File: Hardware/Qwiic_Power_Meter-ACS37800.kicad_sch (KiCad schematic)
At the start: 31 parts, among them J1 Conn_01x01, J10 Conn_01x01, J11 Conn_01x01, J2 Conn_01x04, J3 Qwiic_RA, J4 HI, J5 LO, J6 Conn_01x01, J7 Qwiic_RA, J8 Conn_01x01, J9 Conn_01x01, U1 ACS37800

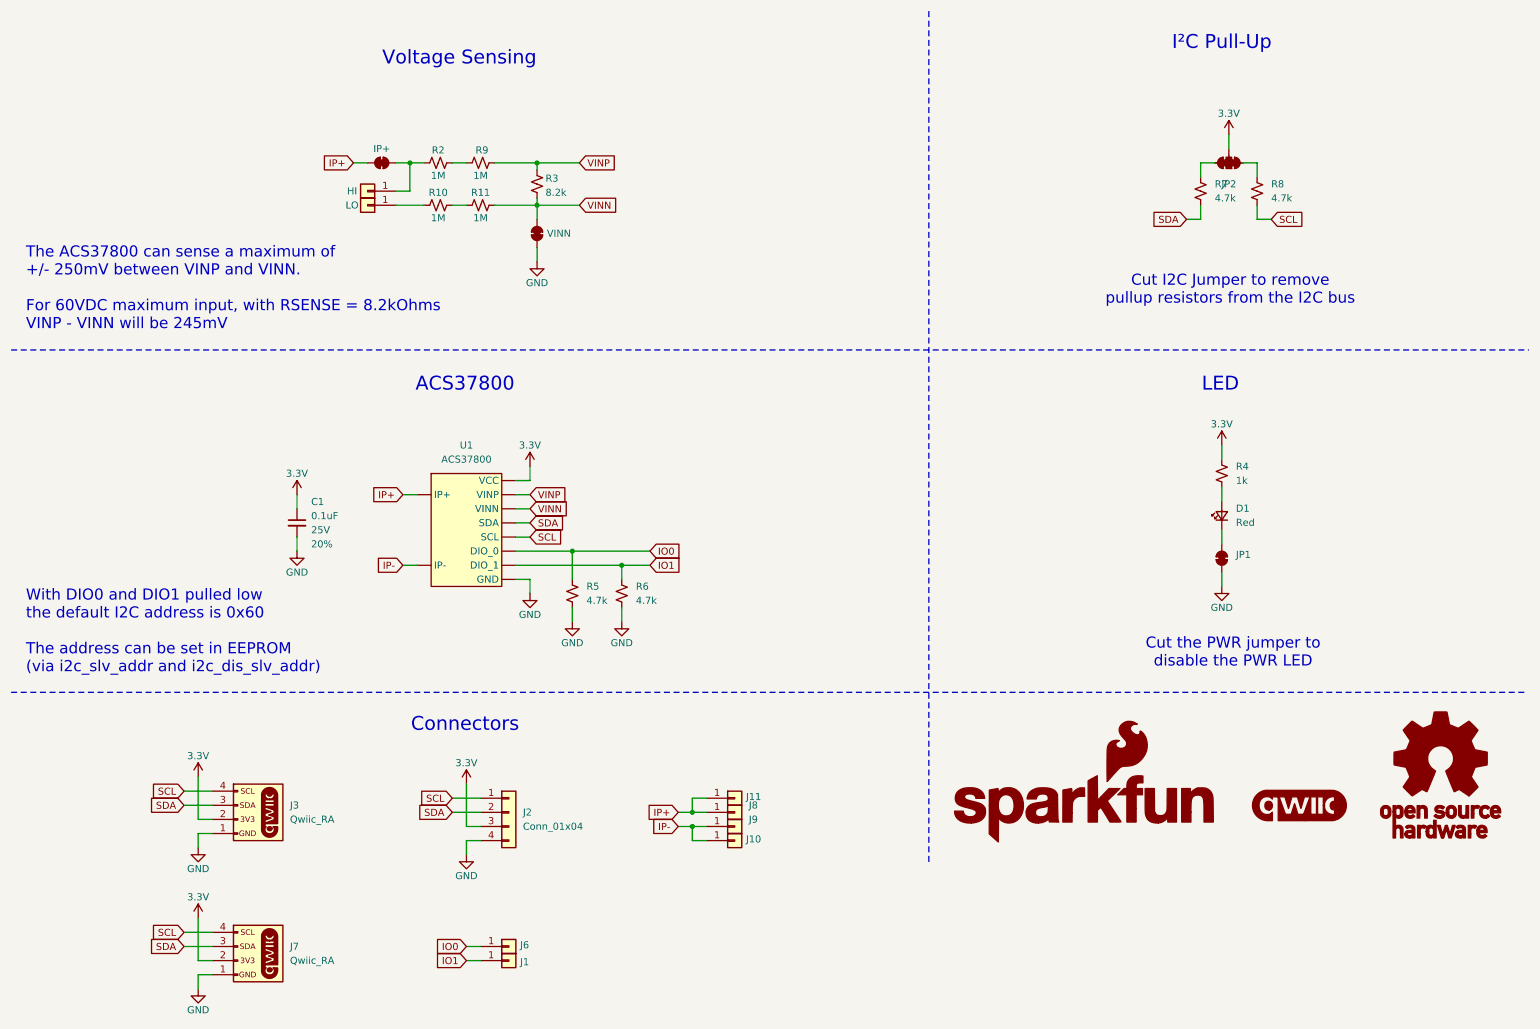
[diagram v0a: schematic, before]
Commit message: Update SOIC Wide footprint
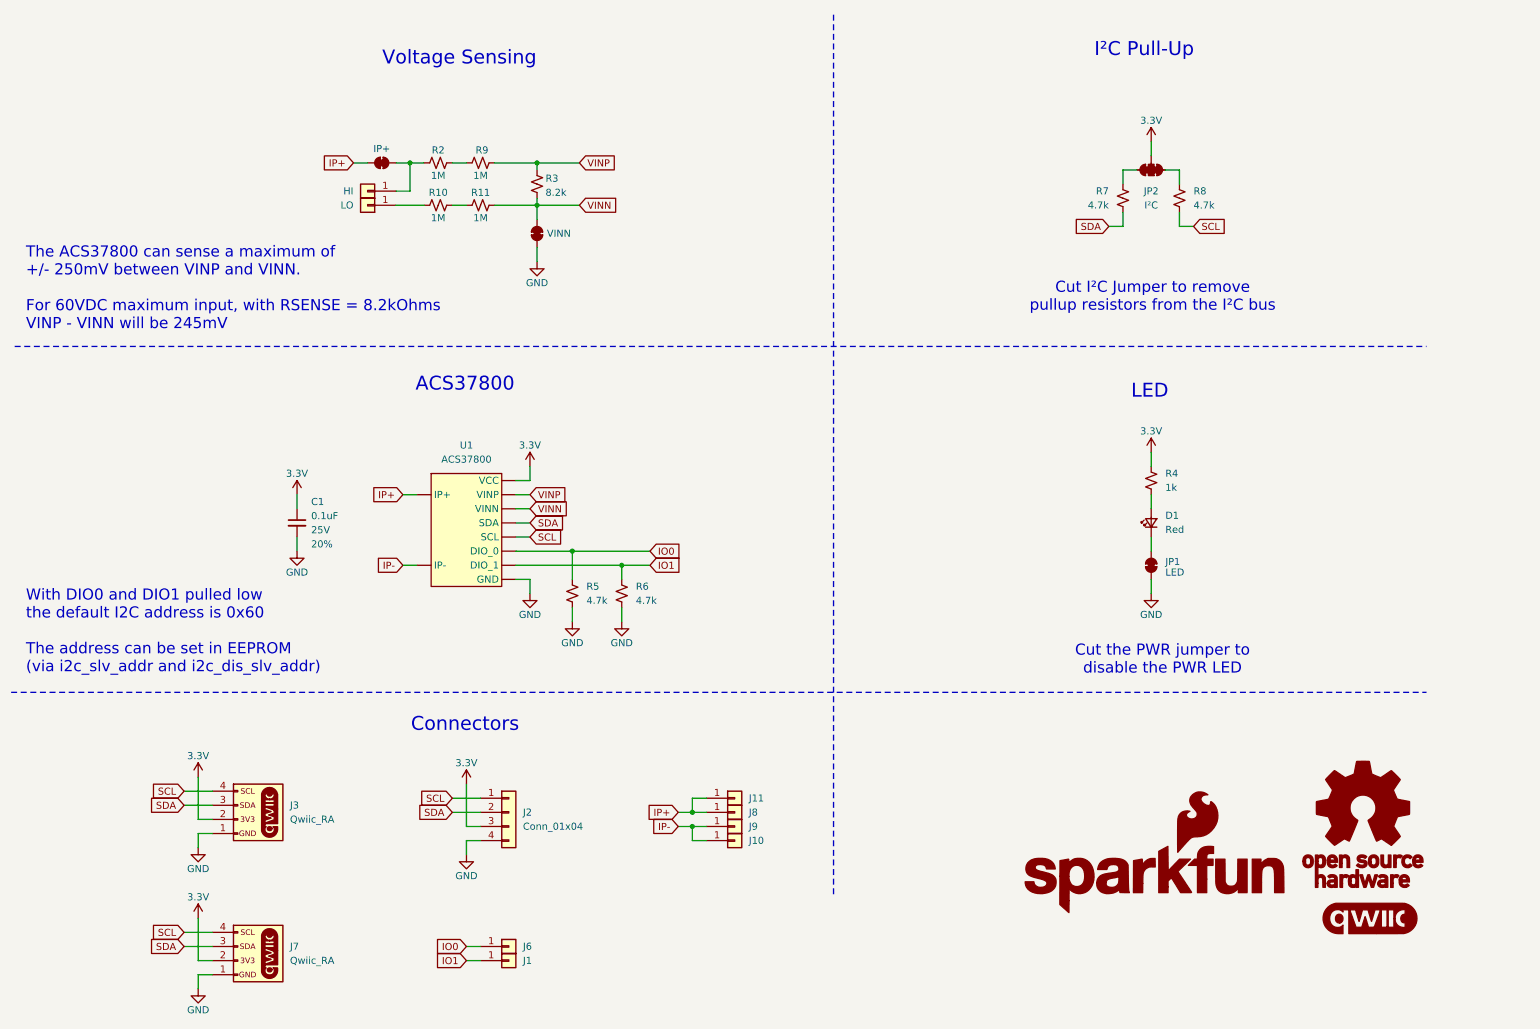
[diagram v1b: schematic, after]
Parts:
- JP1: value ~ -> LED
- JP2: value ~ -> I²C
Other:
- note added: "Cut I²C Jumper to remove pullup resistors from the I²C bus"
- note removed: "Cut I2C Jumper to remove pullup resistors from the I2C bus"
- title: Qwiic Power Meter ACS37800 -> SparkFun Qwiic Power Meter ACS37800
- moved on the sheet: D1, JP1, JP2, R4, R7, R8

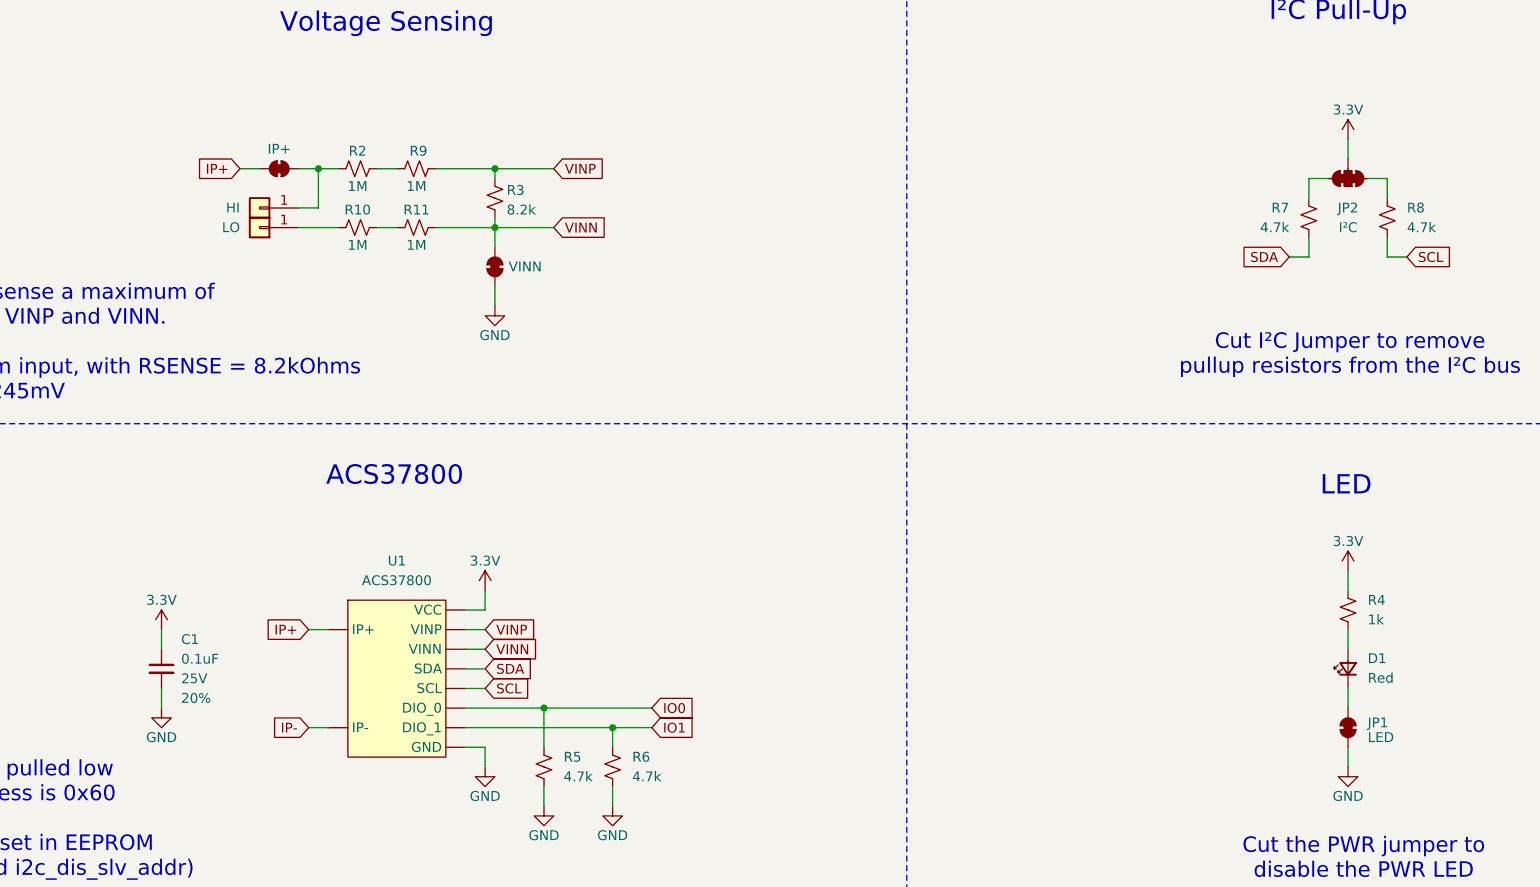
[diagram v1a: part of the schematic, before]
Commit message: Update 0.4in symbol and FP
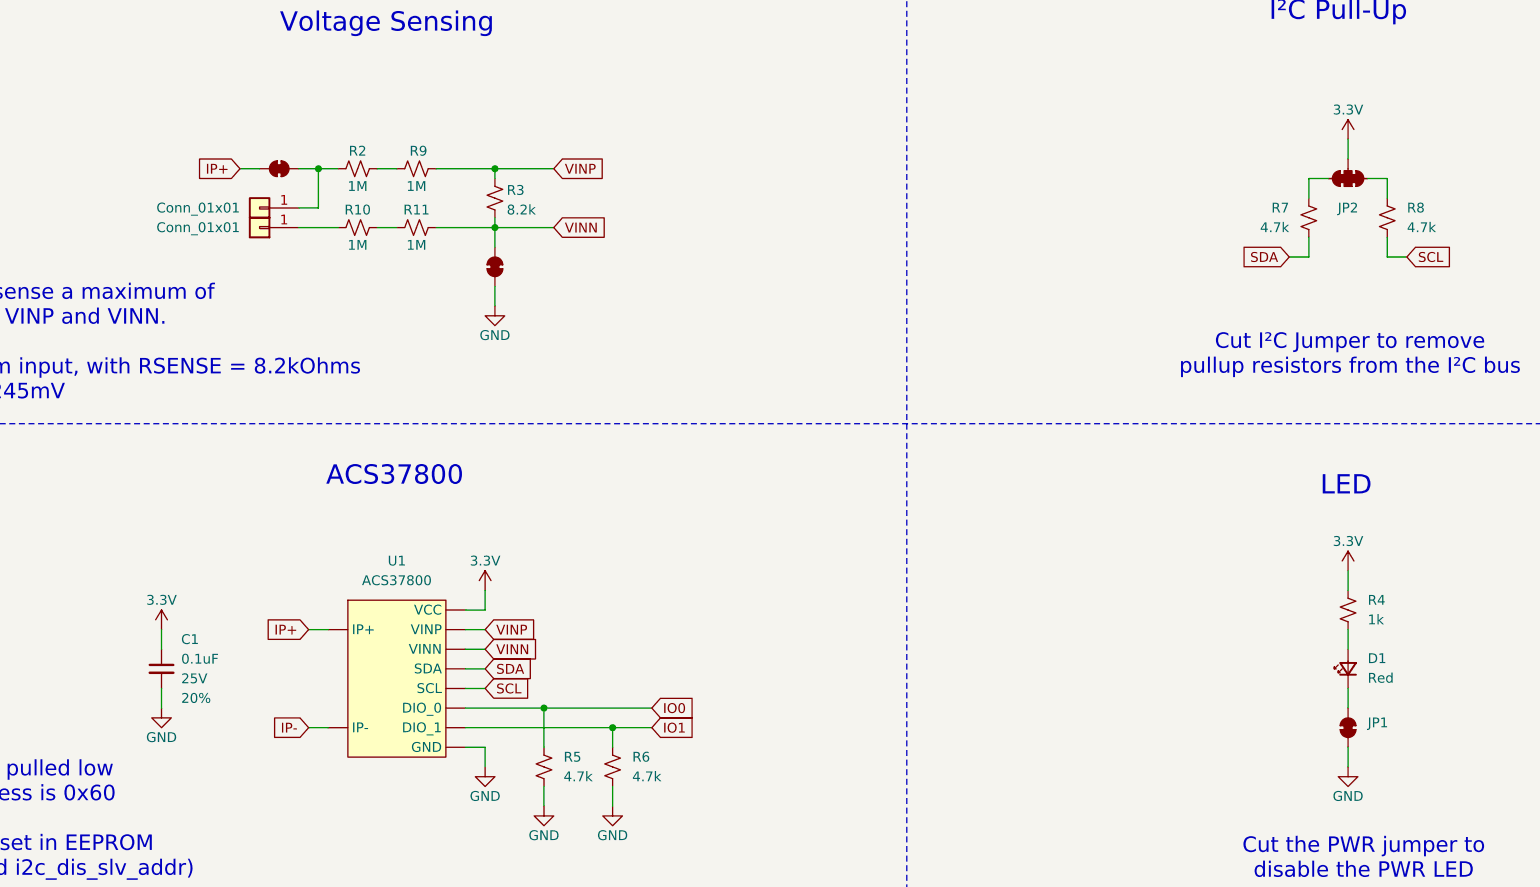
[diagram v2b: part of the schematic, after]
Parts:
- J3, J7: footprint SparkFun-Connector:JST_SMD_1.0mm-4_RA -> SparkFun-Connector:JST_SMD_1.0mm-4_Black
- J4: value HI -> Conn_01x01
- J5: value LO -> Conn_01x01
- J8, J9: footprint SparkFun-Connector:1x01_0.4 -> SparkFun-Connector:1x01_0.4in; symbol SparkFun-Connector:Conn_01x01_0.4 -> SparkFun-Connector:Conn_01x01_0.4in
- JP1: value LED -> ~
- JP2: value I²C -> ~
- JP3: value IP+ -> ~
- JP4: value VINN -> ~
- U1: footprint SparkFun-Semiconductor-Standard:SO-16_WIDE_POWER -> SparkFun-Semiconductor-Standard:SO-16_Wide_Power
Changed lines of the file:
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@@
 	)
 	(symbol
-		(lib_id "SparkFun-Connector:Conn_01x01_0.4")
+		(lib_id "SparkFun-Connector:Conn_01x01_0.4in")
 		(at 142.24 156.21 0)
 		(unit 1)
@@
 			)
 		)
-		(property "Footprint" "SparkFun-Connector:1x01_0.4"
+		(property "Footprint" "SparkFun-Connector:1x01_0.4in"
 			(at 142.24 163.83 0)
 			(effects
@@
 			)
 		)
-		(property "Value" "HI"
+		(property "Value" "Conn_01x01"
 			(at 73.66 44.4499 0)
 			(effects
@@
 			)
 		)
-		(property "Description" "Generic connector, single row, 01x01, script generated (kicad-library-utils/schlib/autogen/connector/)"
+		(property "Description" "Basic 0.1\" PTH"
 			(at 76.2 34.29 0)
 			(effects
@@
 			)
 		)
-		(property "Description" "Generic connector, single row, 01x01, script generated (kicad-library-utils/schlib/autogen/connector/)"
+		(property "Description" "Basic 0.1\" PTH"
 			(at 101.6 190.5 0)
 			(effects
@@
 			)
 		)
-		(property "Description" "Generic connector, single row, 01x01, script generated (kicad-library-utils/schlib/autogen/connector/)"
+		(property "Description" "Basic 0.1\" PTH"
 			(at 142.24 171.45 0)
 			(effects
@@
 			)
 		)
-		(property "Description" "Generic connector, single row, 01x04, script generated (kicad-library-utils/schlib/autogen/connector/)"
+		(property "Description" "Basic 0.1\" PTH"
 			(at 101.6 171.45 0)
 			(effects
@@
 			)
 		)
-		(property "Description" "Generic connector, single row, 01x01, script generated (kicad-library-utils/schlib/autogen/connector/)"
+		(property "Description" "Basic 0.1\" PTH"
 			(at 142.24 163.83 0)
 			(effects
@@
 			)
 		)
-		(property "Value" "I²C"
+		(property "Value" "~"
 			(at 217.17 46.99 0)
 			(effects
@@
 	)
 	(symbol
-		(lib_id "SparkFun-Connector:Conn_01x01_0.4")
+		(lib_id "SparkFun-Connector:Conn_01x01_0.4in")
 		(at 142.24 158.75 0)
 		(unit 1)
@@
 			)
 		)
-		(property "Footprint" "SparkFun-Connector:1x01_0.4"
+		(property "Footprint" "SparkFun-Connector:1x01_0.4in"
 			(at 142.24 166.37 0)
 			(effects
@@
 			)
 		)
-		(property "Footprint" "SparkFun-Connector:JST_SMD_1.0mm-4_RA"
+		(property "Footprint" "SparkFun-Connector:JST_SMD_1.0mm-4_Black"
 			(at 53.34 193.04 0)
 			(effects
@@
 			)
 		)
-		(property "Value" "VINN"
+		(property "Value" "~"
 			(at 108.458 52.07 90)
 			(effects
@@
 			)
 		)
-		(property "Value" "IP+"
+		(property "Value" "~"
 			(at 78.74 36.83 0)
 			(effects
@@
 			)
 		)
-		(property "Footprint" "SparkFun-Connector:JST_SMD_1.0mm-4_RA"
+		(property "Footprint" "SparkFun-Connector:JST_SMD_1.0mm-4_Black"
 			(at 53.34 167.64 0)
 			(effects
@@
 			)
 		)
-		(property "Value" "LED"
+		(property "Value" "~"
 			(at 219.71 113.03 90)
 			(effects
@@
 			)
 		)
-		(property "Footprint" "SparkFun-Semiconductor-Standard:SO-16_WIDE_POWER"
+		(property "Footprint" "SparkFun-Semiconductor-Standard:SO-16_Wide_Power"
 			(at 94.742 124.46 0)
 			(effects
@@
 			)
 		)
-		(property "Value" "LO"
+		(property "Value" "Conn_01x01"
 			(at 73.66 46.9899 0)
 			(effects
@@
 			)
 		)
-		(property "Description" "Generic connector, single row, 01x01, script generated (kicad-library-utils/schlib/autogen/connector/)"
+		(property "Description" "Basic 0.1\" PTH"
 			(at 76.2 36.83 0)
 			(effects
@@
 			)
 		)
-		(property "Description" "Generic connector, single row, 01x01, script generated (kicad-library-utils/schlib/autogen/connector/)"
+		(property "Description" "Basic 0.1\" PTH"
 			(at 101.6 193.04 0)
 			(effects

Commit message: Saved in KiCad 9
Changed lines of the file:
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@@
 (kicad_sch
-	(version 20231120)
+	(version 20250114)
 	(generator "eeschema")
-	(generator_version "8.0")
+	(generator_version "9.0")
 	(paper "USLetter")
 	(title_block
@@
 		(comment 1 "Designed by: Nick Poole")
 	)
+	(text "Voltage Sensing"
+		(exclude_from_sim no)
+		(at 92.71 20.574 0)
+		(effects
+			(font
+				(size 2.5 2.5)
+			)
+		)
+	)
+	(text "Connectors"
+		(exclude_from_sim no)
+		(at 93.726 140.462 0)
+		(effects
+			(font
+				(size 2.5 2.5)
+			)
+		)
+	)
+	(text "The ACS37800 can sense a maximum of\n+/- 250mV between VINP and VINN.\n\nFor 60VDC maximum input, with RSENSE = 8.2kOhms\nVINP - VINN will be 245mV"
+		(exclude_from_sim no)
+		(at 14.732 61.976 0)
+		(effects
+			(font
+				(size 2 2)
+			)
+			(justify left)
+		)
+	)
+	(text "Cut the PWR jumper to\ndisable the PWR LED"
+		(exclude_from_sim no)
+		(at 219.202 128.778 0)
+		(effects
+			(font
+				(size 2 2)
+			)
+		)
+	)
+	(text "With DIO0 and DIO1 pulled low\nthe default I2C address is 0x60\n\nThe address can be set in EEPROM\n(via i2c_slv_addr and i2c_dis_slv_addr)"
+		(exclude_from_sim no)
+		(at 14.732 123.698 0)
+		(effects
+			(font
+				(size 2 2)
+			)
+			(justify left)
+		)
+	)
+	(text "LED"
+		(exclude_from_sim no)
+		(at 216.916 80.518 0)
+		(effects
+			(font
+				(size 2.5 2.5)
+			)
+		)
+	)
+	(text "ACS37800"
+		(exclude_from_sim no)
+		(at 93.726 79.248 0)
+		(effects
+			(font
+				(size 2.5 2.5)
+			)
+		)
+	)
+	(text "I²C Pull-Up"
+		(exclude_from_sim no)
+		(at 215.9 19.05 0)
+		(effects
+			(font
+				(size 2.5 2.5)
+			)
+		)
+	)
+	(text "Cut I²C Jumper to remove \npullup resistors from the I²C bus"
+		(exclude_from_sim no)
+		(at 217.424 63.5 0)
+		(effects
+			(font
+				(size 2 2)
+			)
+		)
+	)
 	(junction
 		(at 134.62 156.21)
@@
 		)
 	)
-	(text "Voltage Sensing"
-		(exclude_from_sim no)
-		(at 92.71 20.574 0)
-		(effects
-			(font
-				(size 2.5 2.5)
-			)
-		)
-	)
-	(text "Connectors"
-		(exclude_from_sim no)
-		(at 93.726 140.462 0)
-		(effects
-			(font
-				(size 2.5 2.5)
-			)
-		)
-	)
-	(text "The ACS37800 can sense a maximum of\n+/- 250mV between VINP and VINN.\n\nFor 60VDC maximum input, with RSENSE = 8.2kOhms\nVINP - VINN will be 245mV"
-		(exclude_from_sim no)
-		(at 14.732 61.976 0)
-		(effects
-			(font
-				(size 2 2)
-			)
-			(justify left)
-		)
-	)
-	(text "Cut the PWR jumper to\ndisable the PWR LED"
-		(exclude_from_sim no)
-		(at 219.202 128.778 0)
-		(effects
-			(font
-				(size 2 2)
-			)
-		)
-	)
-	(text "With DIO0 and DIO1 pulled low\nthe default I2C address is 0x60\n\nThe address can be set in EEPROM\n(via i2c_slv_addr and i2c_dis_slv_addr)"
-		(exclude_from_sim no)
-		(at 14.732 123.698 0)
-		(effects
-			(font
-				(size 2 2)
-			)
-			(justify left)
-		)
-	)
-	(text "LED"
-		(exclude_from_sim no)
-		(at 216.916 80.518 0)
-		(effects
-			(font
-				(size 2.5 2.5)
-			)
-		)
-	)
-	(text "ACS37800"
-		(exclude_from_sim no)
-		(at 93.726 79.248 0)
-		(effects
-			(font
-				(size 2.5 2.5)
-			)
-		)
-	)
-	(text "I²C Pull-Up"
-		(exclude_from_sim no)
-		(at 215.9 19.05 0)
-		(effects
-			(font
-				(size 2.5 2.5)
-			)
-		)
-	)
-	(text "Cut I²C Jumper to remove \npullup resistors from the I²C bus"
-		(exclude_from_sim no)
-		(at 217.424 63.5 0)
-		(effects
-			(font
-				(size 2 2)
-			)
-		)
-	)
 	(global_label "SDA"
 		(shape input)
@@
 		)
 	)
+	(embedded_fonts no)
 )
